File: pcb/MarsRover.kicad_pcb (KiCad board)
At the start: 2 copper layers, 60 x 52 mm, 45 parts, among them J2 JST-PH 2,0, M1 Vibrationsmotor links, M2 Vibrationsmotor rechts, Q1 AO3400A, Q2 AO3400A, U1 ESP32-DevKitC V4, U2 TP4056-Modul, U5 MT3608 auf 5,00V, U6 GY-521 MPU-6050, U7 GY-530 VL53L0X

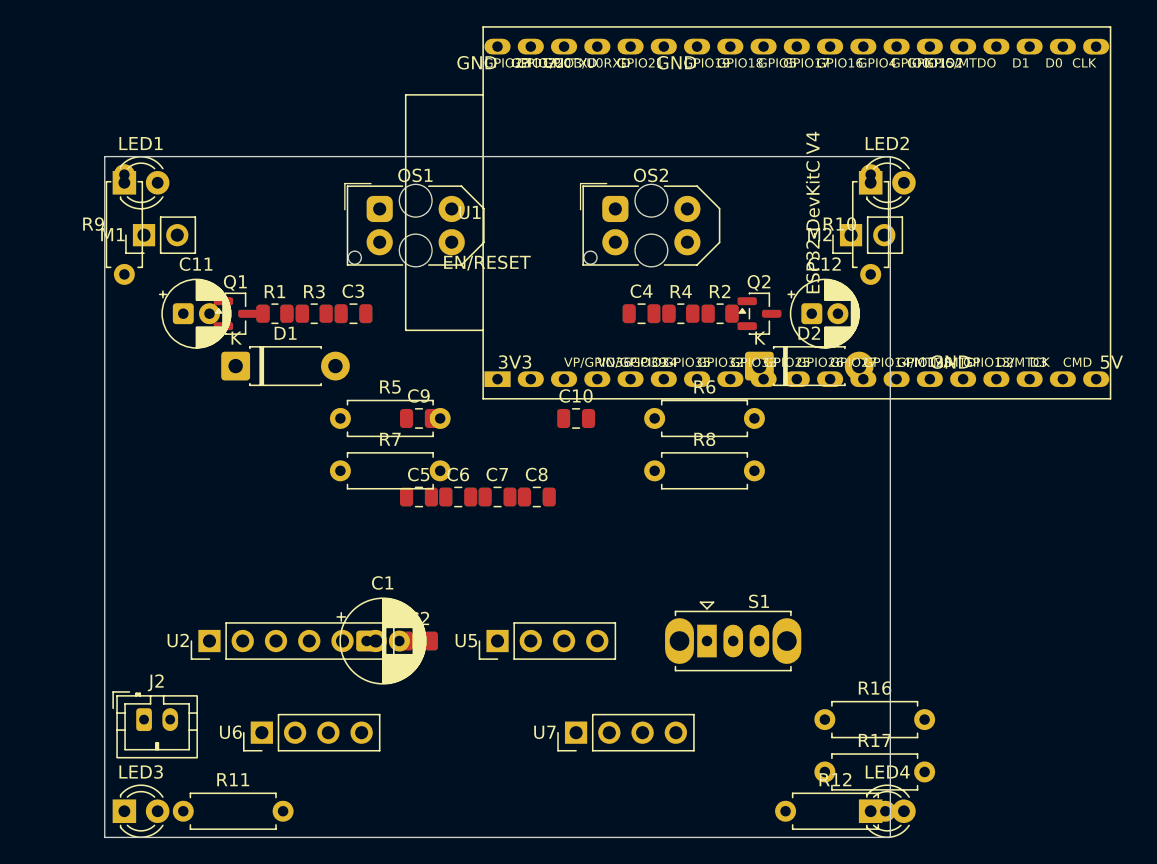
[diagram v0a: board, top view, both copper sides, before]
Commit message: Layout Version A: 70 x 52 mm, alles platziert, null ernste DRC-Fehler
Schaltplan: die doppelt vergebenen Power-Referenzen #PWR34 und #PWR36
entwirrt. Mein Einfuegeskript hatte mit dem Zaehlen neu angefangen,
obwohl der urspruengliche Aufbau diese Nummern schon benutzte. Das war
der Fehler, den KiCads Annotation gemeldet hat. ERC weiter 0 Fehler.

Platine:
  Kontur 70 x 52 mm (Version A). Breiter heisst mehr Lenkautoritaet --
  das Lenkmoment ist Vibrationskraft mal Abstand zur Laengsachse.
  Entwurfsregeln: Abstand 0,2 mm, Bahn 0,4 mm, minimal 0,25 mm,
  Durchkontaktierung 0,8/0,4 mm.
  Netzklasse "Leistung" mit 1,0 mm fuer +5V, +3V3, GND, Akkupfad und
  die beiden Motorzweige.

  Anordnung:
    vorn      Liniensensoren auf der UNTERSEITE, gelbe LEDs aussen,
              Motor-Loetaugen weit aussen, daneben die Puffer-Elkos
    links     Finne TP4056, rechts Finne MT3608 -- die Module stehen
              senkrecht auf ihren Loetaugenreihen
    Mitte     ESP32 quer; seine Padreihen liegen bei y 72,30 und 97,70,
              der 22 mm hohe Korridor dazwischen nimmt alles Flache auf
    hinten    JST, C1, GY-521, GY-530, Schalter, Teiler, rote LEDs

  C11 und C12 muessten eigentlich zu den Motorstufen, sind als
  Radialtyp aber rund 11 mm hoch und passen nicht unter die gesteckte
  Platine (gut 8,5 mm). Sie stehen jetzt vorn neben den Motor-Loetaugen
  -- elektrisch der bessere Platz, naeher an der Last.

DRC: 202 Meldungen, davon 0 ernst. Der Rest ist Siebdruck-Ueberlappung,
Textgroesse und Courtyard-Ueberschneidungen unter dem DevKit -- letztere
sind gewollt, KiCad kennt die 8,5 mm Bauhoehe der Buchsenleisten nicht.

Noch nicht geroutet.

Co-Authored-By: Claude Opus 5 <noreply@anthropic.com>
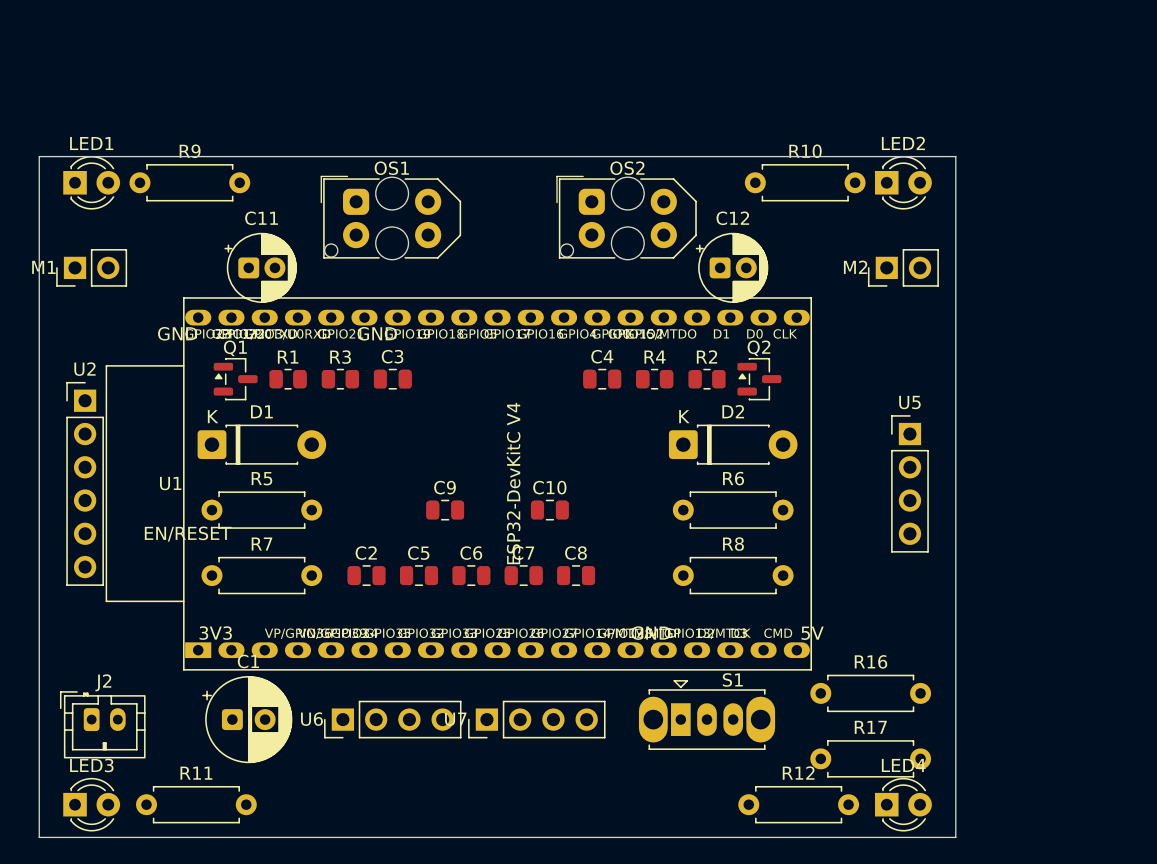
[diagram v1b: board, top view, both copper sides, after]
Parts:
- moved U5 35.2 mm to (161.5, 81.2), turned to 0 degrees
- moved U1 30.8 mm to (107.1, 97.7)
- moved U2 20.7 mm to (98.5, 78.7), turned to 0 degrees
- moved R7 12.7 mm to (108.2, 92.0)
- moved R5 12.1 mm to (108.2, 87.0)
- moved C1 11.9 mm to (109.8, 103.0)
- moved R10 11.3 mm to (149.7, 62.0), turned to 0 degrees
- moved D2 8.35 mm to (144.2, 82.0)
- moved R8 8.29 mm to (144.2, 92.0)
- moved C12 7.83 mm to (147.0, 68.5)
- moved R6 7.33 mm to (144.2, 87.0)
- moved C10 7.28 mm to (134.0, 87.0)
- moved C9 7.28 mm to (126.0, 87.0)
- moved R9 7.10 mm to (102.7, 62.0), turned to 0 degrees
- moved U7 6.88 mm to (129.2, 103.0)
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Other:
- board size 60 x 52 mm -> 70 x 52 mm

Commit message: Platine geroutet: 27 von 27 Netzen, null unverbundene Elemente
Geroutet mit KiCadRoutingTools (A*-Router mit Rust-Kern, MIT, headless auf
der .kicad_pcb). 101 Durchkontaktierungen, Massflaeche auf B.Cu als eine
zusammenhaengende Insel. DRC: 0 Abstandsverstoesse, 0 Kurzschluesse,
0 unverbundene Elemente; es bleiben nur Siebdruck-Kosmetik und die
gewollten Courtyard-Ueberlappungen unter dem gesockelten DevKit.

Platzierung nachgezogen:
- J2 liegend (S2B-PH-K) auf die Unterseite, der Akku kommt darunter
- OS1/OS2 Fototransistoren nach innen, optische Messflecken 18 mm
  auseinander -- im Fenster 15..20 mm fuer ein 19-mm-Band
- U6 hinten mittig, waagerecht montierbar, Gyro-Z bleibt die Hochachse
- S1 daneben
- R2 und Q2 nach aussen: R2 Pad 1 hatte beidseitig nur 0,8 mm Padabstand,
  genau die Breite einer 0,4-mm-Leitung mit Abstand -- daran scheiterten
  zwei Router nacheinander

Kein Ausschnitt fuer den MPU-6050: ein Gyro misst die Drehrate ueberall
gleich, und die Zentrifugalterme liegen bei 0,03 g, zwei Groessenordnungen
unter der Motorvibration. Das Loch haette Steifigkeit und Massflaeche
gekostet, ohne messbar etwas zu bringen.

Netzklassen gesetzt: Default 0,4 mm / Leistung 1,0 mm, Abstand 0,2 mm.

Co-Authored-By: Claude Opus 5 <noreply@anthropic.com>
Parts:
- J2: footprint Connector_JST:JST_PH_B2B-PH-K_1x02_P2.00mm_Vertical -> JST_PH_S2B-PH-K_1x02_P2.00mm_Horizontal; moved to B.Cu
- R1, R2, R3, R4: footprint Resistor_SMD:R_0805_2012Metric -> Resistor_SMD:R_0805_2012Metric_Pad1.20x1.40mm_HandSolder
- R16, R17, R5, R6, R7, R8: footprint Resistor_THT:R_Axial_DIN0207_L6.3mm_D2.5mm_P7.62mm_Horizontal -> Resistor_SMD:R_0805_2012Metric_Pad1.20x1.40mm_HandSolder
- moved U7 35.1 mm to (126.2, 68.0)
- moved U6 8.00 mm to (126.2, 103.0)
- moved S1 7.21 mm to (140.0, 109.0)
- moved R17 6.14 mm to (160.5, 104.0), turned to -90 degrees
- moved OS2 4.57 mm to (141.8, 63.0), turned to 180 degrees
- moved R16 3.50 mm to (156.5, 104.0), turned to 90 degrees
- moved J2 3.35 mm to (100.5, 100.0), turned to 180 degrees
- moved OS1 2.30 mm to (118.2, 65.5)
- moved C11 1.00 mm to (111.0, 67.5)
- moved C12 1.00 mm to (147.0, 67.5)
- moved LED1 0.60 mm to (97.7, 62.6)
- moved LED2 0.60 mm to (159.7, 62.6)
- moved R10 0.60 mm to (149.7, 62.6)
- moved R9 0.60 mm to (102.7, 62.6)
- moved Q2 0.60 mm to (150.6, 77.0)
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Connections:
- C1 pad 1: GND -> +5V
- C2 pad 1: GND -> +5V
- C5 pad 1: (no net) -> +5V
- C5 pad 2: (no net) -> GND
- C6 pad 2: (no net) -> GND
- R16 pad 1: (no net) -> Net-(S1-B)
- S1 pad 2: Net-(S1-Pad2) -> Net-(S1-B)
- S1 pad 3: (no net) -> unconnected-(S1-C-Pad3)
- U1 pad 13: (no net) -> unconnected-(U1-MTDI/GPIO12/ADC2_CH5-Pad13)
- U1 pad 15: (no net) -> unconnected-(U1-MTCK/GPIO13/ADC2_CH4-Pad15)
- U1 pad 16: (no net) -> unconnected-(U1-SD_DATA2/GPIO9-Pad16)
- U1 pad 17: (no net) -> unconnected-(U1-SD_DATA3/GPIO10-Pad17)
- U1 pad 18: (no net) -> unconnected-(U1-CMD-Pad18)
- U1 pad 2: (no net) -> unconnected-(U1-CHIP_PU-Pad2)
- U1 pad 20: (no net) -> unconnected-(U1-SD_CLK/GPIO6-Pad20)
- U1 pad 21: (no net) -> unconnected-(U1-SD_DATA0/GPIO7-Pad21)
- U1 pad 22: (no net) -> unconnected-(U1-SD_DATA1/GPIO8-Pad22)
- U1 pad 23: (no net) -> unconnected-(U1-MTDO/GPIO15/ADC2_CH3-Pad23)
- U1 pad 24: (no net) -> unconnected-(U1-ADC2_CH2/GPIO2-Pad24)
- U1 pad 25: (no net) -> unconnected-(U1-GPIO0/BOOT/ADC2_CH1-Pad25)
- U1 pad 26: (no net) -> unconnected-(U1-ADC2_CH0/GPIO4-Pad26)
- U1 pad 27: (no net) -> unconnected-(U1-GPIO16-Pad27)
- U1 pad 28: (no net) -> unconnected-(U1-GPIO17-Pad28)
- U1 pad 29: (no net) -> unconnected-(U1-GPIO5-Pad29)
- U1 pad 3: (no net) -> unconnected-(U1-SENSOR_VP/GPIO36/ADC1_CH0-Pad3)
- U1 pad 30: (no net) -> unconnected-(U1-GPIO18-Pad30)
- U1 pad 31: (no net) -> unconnected-(U1-GPIO19-Pad31)
- U1 pad 34: (no net) -> unconnected-(U1-U0RXD/GPIO3-Pad34)
- U1 pad 35: (no net) -> unconnected-(U1-U0TXD/GPIO1-Pad35)
- U1 pad 36: (no net) -> Net-(U1-GPIO22)
- U1 pad 37: (no net) -> unconnected-(U1-GPIO23-Pad37)
- U2 pad 1: (no net) -> unconnected-(U2-Pin_1-Pad1)
- U2 pad 5: Net-(S1-Pad2) -> Net-(S1-B)
- U5 pad 3: GND -> +5V
- U6 pad 3: Net-(U6-Pad3) -> Net-(U1-GPIO22)
- U7 pad 3: Net-(U6-Pad3) -> Net-(U1-GPIO22)
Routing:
- net +5V: track 0.00 -> 193.2 mm, vias 0 -> 16
- net +3V3: track 0.00 -> 176.7 mm, vias 0 -> 15
- net Net-(OS2-E): track 0.00 -> 97.9 mm, vias 0 -> 3
- net Net-(U1-GPIO21): track 0.00 -> 86.8 mm, vias 0 -> 4
- net Net-(S1-B): track 0.00 -> 85.0 mm, vias 0 -> 5
- net Net-(U1-GPIO22): track 0.00 -> 79.2 mm, vias 0 -> 2
- net Net-(U1-MTMS/GPIO14/ADC2_CH6): track 0.00 -> 75.8 mm, vias 0 -> 2
- net GND: track 0.00 -> 66.3 mm, vias 0 -> 14
- net Net-(OS1-E): track 0.00 -> 62.5 mm, vias 0 -> 7
- net Net-(U1-ADC2_CH7/GPIO27): track 0.00 -> 60.1 mm, vias 0 -> 3
- net Net-(U1-SENSOR_VN/GPIO39/ADC1_CH3): track 0.00 -> 58.2 mm, vias 0 -> 4
- net Net-(U1-DAC_2/ADC2_CH9/GPIO26): track 0.00 -> 43.8 mm
- net Net-(U1-DAC_1/ADC2_CH8/GPIO25): track 0.00 -> 43.4 mm, vias 0 -> 2
- net Net-(S1-A): track 0.00 -> 39.7 mm
- net Net-(OS2-A): track 0.00 -> 37.2 mm, vias 0 -> 2
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- added copper zone on B.Cu, net GND

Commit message: U5 an die Hinterkante: der Micro-USB des DevKits war blockiert
Pad 1 von U1 ist 3V3 (Antennenende), Pad 19 ist 5V -- der USB sitzt also am
+x-Ende bei x = 154, mittig auf der Modulbreite bei y = 85. U5 stand mit
y 81,2..88,8 genau davor.

U5 jetzt bei y 97,0..104,62, Gehaeusevorderkante 95,2 -- gut 4 mm Luft zum
Steckergehaeuse. Damit das ging, mussten R16/R17 (Spannungsteiler VBAT ->
GPIO39) von x 156,5/160,5 nach x 150/154 wandern; als 0805 duerfen sie
ueberall in den hinteren Streifen.

Neu geroutet: 27/27 Netze, 91/91 Padpaare, 91 Durchkontaktierungen, keine
in einem Pad. DRC: 0 unverbundene Elemente, 0 Abstandsverstoesse, 0 lose
Leitungsenden.

Co-Authored-By: Claude Opus 5 <noreply@anthropic.com>
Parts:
- moved U5 15.8 mm to (161.5, 97.0)
- moved R16 6.50 mm to (150.0, 104.0)
- moved R17 6.50 mm to (154.0, 104.0)
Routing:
- net GND: track 66.3 -> 96.1 mm, vias 14 -> 15
- net +3V3: track 176.7 -> 201.8 mm, vias 15 -> 14
- net +5V: track 193.2 -> 213.3 mm
- net Net-(S1-A): track 39.7 -> 25.6 mm
- net Net-(U1-MTMS/GPIO14/ADC2_CH6): track 75.8 -> 68.5 mm, vias 2 -> 3
- net Net-(S1-B): track 85.0 -> 77.9 mm
- net Net-(OS1-E): track 62.5 -> 60.9 mm, vias 7 -> 6
- net Net-(D2-A): track 35.4 -> 33.9 mm, vias 1 -> 2
- net Net-(U1-GPIO21): track 86.8 -> 87.9 mm
- net Net-(U1-ADC2_CH7/GPIO27): track 60.1 -> 59.3 mm, vias 3 -> 5
- net Net-(U1-GPIO22): track 79.2 -> 78.5 mm
- net Net-(U1-32K_XN/GPIO33/ADC1_CH5): track 31.5 -> 30.8 mm, vias 1 -> 0
- net Net-(U1-SENSOR_VN/GPIO39/ADC1_CH3): track 58.2 -> 57.7 mm, vias 4 -> 5
- net Net-(OS2-E): track 97.9 -> 97.6 mm, vias 3 -> 6
- net Net-(D1-A): track 34.7 -> 34.9 mm, vias 3 -> 2
